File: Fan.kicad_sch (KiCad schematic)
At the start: 23 parts, among them M1 Fan_4pin, M2 Fan_4pin

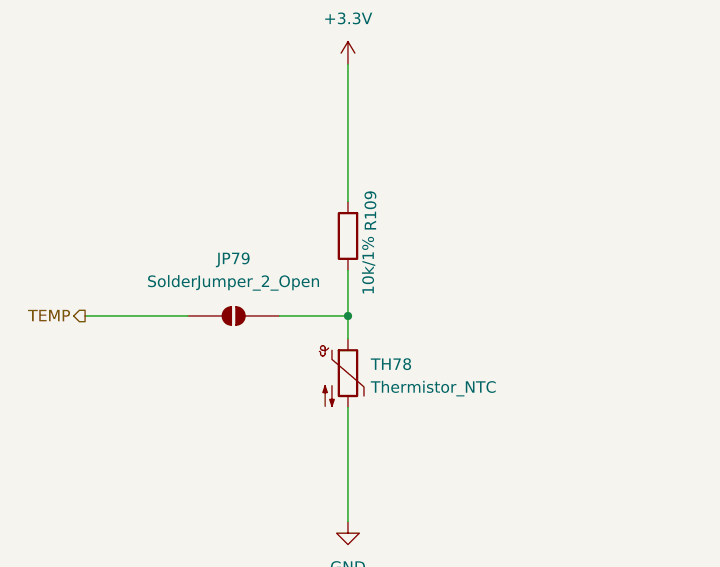
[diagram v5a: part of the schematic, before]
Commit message: Designators in PSU restored
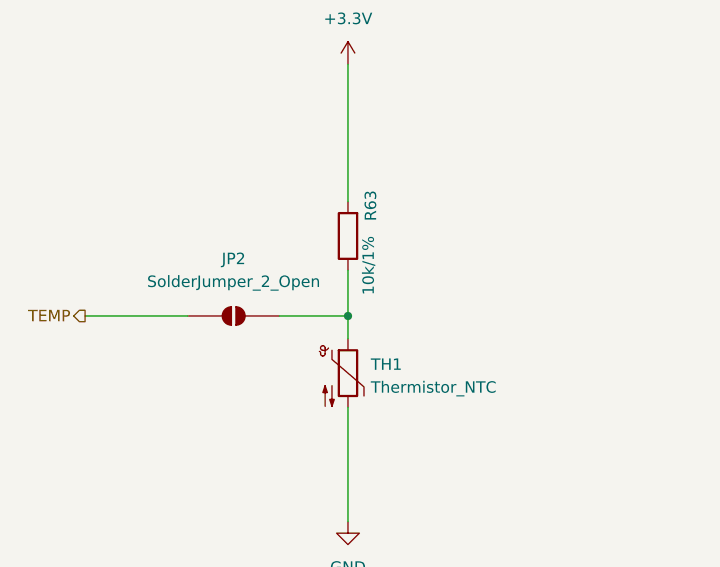
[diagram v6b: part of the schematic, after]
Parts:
- renumbered JP79 to JP2, R109 to R63, TH78 to TH1
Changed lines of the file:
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@@
 		(dnp no)
 		(fields_autoplaced yes)
-		(property "Reference" "TH78"
+		(property "Reference" "TH1"
 			(at 58.42 90.4874 0)
 			(show_name no)
@@
 			(project "Carrier_Board"
 				(path "/e768274e-12f3-4f83-96f6-abb7638e0bc1/db5534e0-ad9a-443b-b9b9-b696f6fb2c85"
-					(reference "TH78")
+					(reference "TH1")
 					(unit 1)
 				)
@@
 		(dnp no)
 		(fields_autoplaced yes)
-		(property "Reference" "JP79"
+		(property "Reference" "JP2"
 			(at 43.18 78.74 0)
 			(show_name no)
@@
 			(project "Carrier_Board"
 				(path "/e768274e-12f3-4f83-96f6-abb7638e0bc1/db5534e0-ad9a-443b-b9b9-b696f6fb2c85"
-					(reference "JP79")
+					(reference "JP2")
 					(unit 1)
 				)
@@
 		(in_pos_files yes)
 		(dnp no)
-		(property "Reference" "R109"
+		(property "Reference" "R63"
 			(at 58.42 71.12 90)
 			(show_name no)
@@
 			(project "Carrier_Board"
 				(path "/e768274e-12f3-4f83-96f6-abb7638e0bc1/db5534e0-ad9a-443b-b9b9-b696f6fb2c85"
-					(reference "R109")
+					(reference "R63")
 					(unit 1)
 				)
